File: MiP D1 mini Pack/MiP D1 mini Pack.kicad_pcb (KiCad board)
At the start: 2 copper layers, 41.4 x 63.8 mm, 15 parts, among them J1 MiP, J2 Debug, U1 WEMOS D1 mini, U2 74LVC1G125

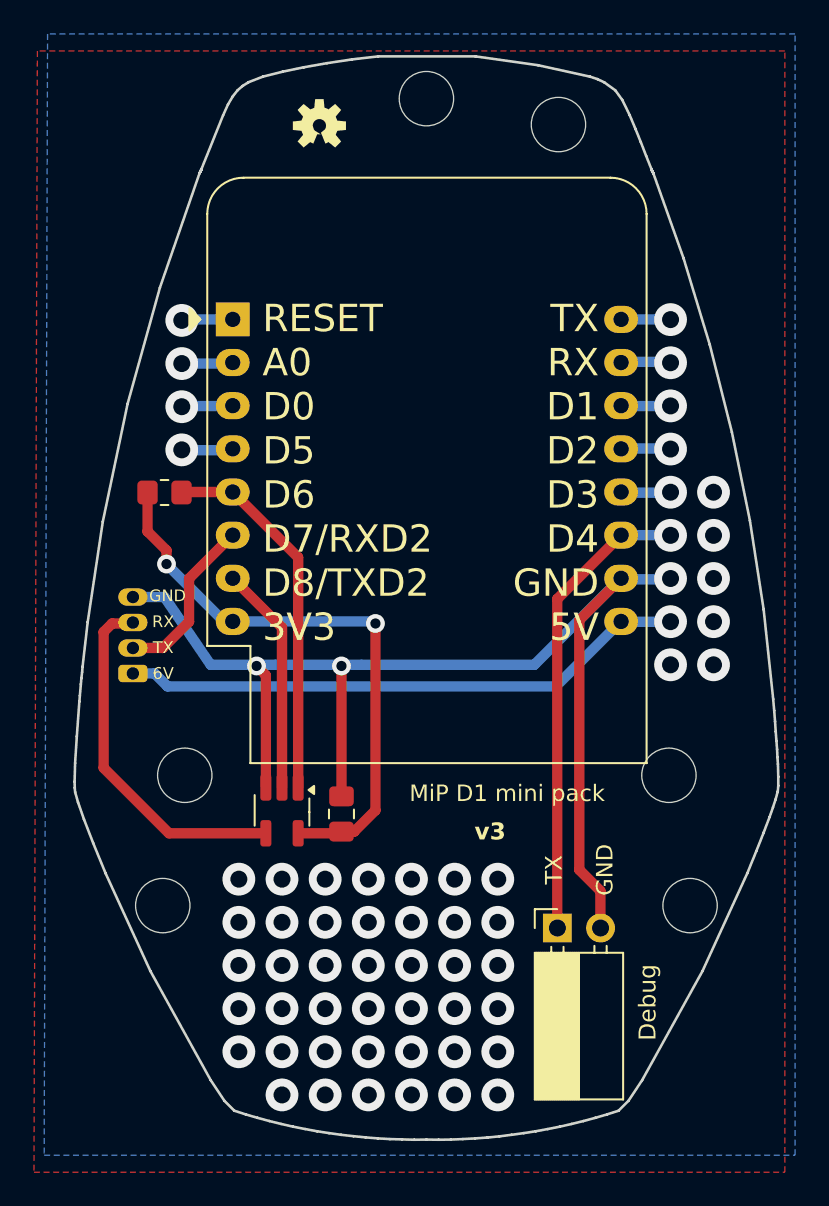
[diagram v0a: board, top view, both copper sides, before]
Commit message: Prototyping area
Figured out adding prototyping areas.
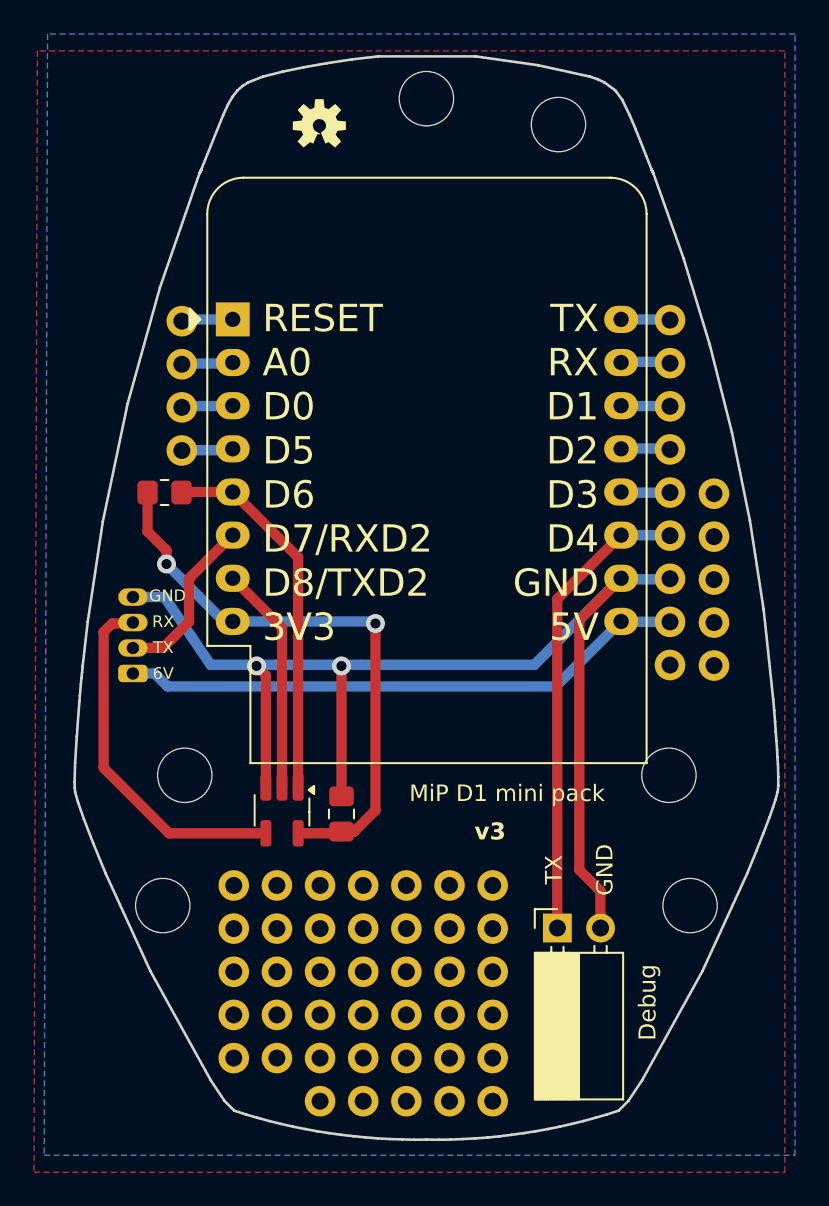
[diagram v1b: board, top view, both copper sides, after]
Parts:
- added REF**: Prototype pad, Tiogaplanet_Library:Prototype pad, F.Cu at (144.8, 124.5)
- added REF**: Prototype pad, Tiogaplanet_Library:Prototype pad, F.Cu at (139.7, 132.1)
- added REF**: Prototype pad, Tiogaplanet_Library:Prototype pad, F.Cu at (139.7, 129.5)
- added REF**: Prototype pad, Tiogaplanet_Library:Prototype pad, F.Cu at (134.1, 96.3)
- added REF**: Prototype pad, Tiogaplanet_Library:Prototype pad, F.Cu at (139.7, 121.9)
- added REF**: Prototype pad, Tiogaplanet_Library:Prototype pad, F.Cu at (144.8, 132.1)
- added REF**: Prototype pad, Tiogaplanet_Library:Prototype pad, F.Cu at (149.9, 121.9)
- added REF**: Prototype pad, Tiogaplanet_Library:Prototype pad, F.Cu at (149.9, 127.0)
- added REF**: Prototype pad, Tiogaplanet_Library:Prototype pad, F.Cu at (139.7, 124.5)
- added REF**: Prototype pad, Tiogaplanet_Library:Prototype pad, F.Cu at (152.4, 124.5)
- added REF**: Prototype pad, Tiogaplanet_Library:Prototype pad, F.Cu at (137.2, 124.5)
- added REF**: Prototype pad, Tiogaplanet_Library:Prototype pad, F.Cu at (162.8, 101.3)
- added REF**: Prototype pad, Tiogaplanet_Library:Prototype pad, F.Cu at (144.8, 121.9)
- added REF**: Prototype pad, Tiogaplanet_Library:Prototype pad, F.Cu at (165.4, 106.4)
- added REF**: Prototype pad, Tiogaplanet_Library:Prototype pad, F.Cu at (162.8, 108.9)
- added REF**: Prototype pad, Tiogaplanet_Library:Prototype pad, F.Cu at (152.4, 134.6)
- added REF**: Prototype pad, Tiogaplanet_Library:Prototype pad, F.Cu at (162.8, 88.6)
- added REF**: Prototype pad, Tiogaplanet_Library:Prototype pad, F.Cu at (144.8, 127.0)
- added REF**: Prototype pad, Tiogaplanet_Library:Prototype pad, F.Cu at (162.8, 91.2)
- added REF**: Prototype pad, Tiogaplanet_Library:Prototype pad, F.Cu at (152.4, 132.1)
- added REF**: Prototype pad, Tiogaplanet_Library:Prototype pad, F.Cu at (162.8, 93.7)
- added REF**: Prototype pad, Tiogaplanet_Library:Prototype pad, F.Cu at (149.9, 132.1)
- added REF**: Prototype pad, Tiogaplanet_Library:Prototype pad, F.Cu at (144.8, 129.5)
- added REF**: Prototype pad, Tiogaplanet_Library:Prototype pad, F.Cu at (142.2, 134.6)
- added REF**: Prototype pad, Tiogaplanet_Library:Prototype pad, F.Cu at (147.3, 124.5)
- added REF**: Prototype pad, Tiogaplanet_Library:Prototype pad, F.Cu at (147.3, 121.9)
- added REF**: Prototype pad, Tiogaplanet_Library:Prototype pad, F.Cu at (165.4, 109.0)
- added REF**: Prototype pad, Tiogaplanet_Library:Prototype pad, F.Cu at (162.8, 98.8)
- added REF**: Prototype pad, Tiogaplanet_Library:Prototype pad, F.Cu at (147.3, 129.5)
- added REF**: Prototype pad, Tiogaplanet_Library:Prototype pad, F.Cu at (134.1, 93.8)
- added REF**: Prototype pad, Tiogaplanet_Library:Prototype pad, F.Cu at (147.3, 132.1)
- added REF**: Prototype pad, Tiogaplanet_Library:Prototype pad, F.Cu at (162.8, 103.9)
- added REF**: Prototype pad, Tiogaplanet_Library:Prototype pad, F.Cu at (147.3, 127.0)
- added REF**: Prototype pad, Tiogaplanet_Library:Prototype pad, F.Cu at (137.2, 129.5)
- added REF**: Prototype pad, Tiogaplanet_Library:Prototype pad, F.Cu at (142.2, 121.9)
- added REF**: Prototype pad, Tiogaplanet_Library:Prototype pad, F.Cu at (139.7, 127.0)
- added REF**: Prototype pad, Tiogaplanet_Library:Prototype pad, F.Cu at (149.9, 124.5)
- added REF**: Prototype pad, Tiogaplanet_Library:Prototype pad, F.Cu at (149.9, 134.6)
- added REF**: Prototype pad, Tiogaplanet_Library:Prototype pad, F.Cu at (152.4, 121.9)
- added REF**: Prototype pad, Tiogaplanet_Library:Prototype pad, F.Cu at (137.2, 121.9)
- added REF**: Prototype pad, Tiogaplanet_Library:Prototype pad, F.Cu at (137.2, 132.1)
- added REF**: Prototype pad, Tiogaplanet_Library:Prototype pad, F.Cu at (147.3, 134.6)
- added REF**: Prototype pad, Tiogaplanet_Library:Prototype pad, F.Cu at (142.2, 129.5)
- added REF**: Prototype pad, Tiogaplanet_Library:Prototype pad, F.Cu at (152.4, 129.5)
- added REF**: Prototype pad, Tiogaplanet_Library:Prototype pad, F.Cu at (137.2, 127.0)
- added REF**: Prototype pad, Tiogaplanet_Library:Prototype pad, F.Cu at (165.4, 103.9)
- added REF**: Prototype pad, Tiogaplanet_Library:Prototype pad, F.Cu at (165.4, 101.4)
- added REF**: Prototype pad, Tiogaplanet_Library:Prototype pad, F.Cu at (142.2, 132.1)
- added REF**: Prototype pad, Tiogaplanet_Library:Prototype pad, F.Cu at (134.1, 91.2)
- added REF**: Prototype pad, Tiogaplanet_Library:Prototype pad, F.Cu at (149.9, 129.5)
- added REF**: Prototype pad, Tiogaplanet_Library:Prototype pad, F.Cu at (142.2, 127.0)
- added REF**: Prototype pad, Tiogaplanet_Library:Prototype pad, F.Cu at (142.2, 124.5)
- added REF**: Prototype pad, Tiogaplanet_Library:Prototype pad, F.Cu at (162.8, 106.4)
- added REF**: Prototype pad, Tiogaplanet_Library:Prototype pad, F.Cu at (134.1, 88.7)
- added REF**: Prototype pad, Tiogaplanet_Library:Prototype pad, F.Cu at (162.8, 96.3)
- added REF**: Prototype pad, Tiogaplanet_Library:Prototype pad, F.Cu at (144.8, 134.6)
- added REF**: Prototype pad, Tiogaplanet_Library:Prototype pad, F.Cu at (165.4, 98.9)
- added REF**: Prototype pad, Tiogaplanet_Library:Prototype pad, F.Cu at (152.4, 127.0)
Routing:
- net unconnected-(U1-~{RST}-Pad1): track 3.02 -> 2.94 mm, vias 1 -> 0
- net unconnected-(U1-TX-Pad16): vias 1 -> 0
- net unconnected-(U1-SDA/D2-Pad13): vias 1 -> 0
- net unconnected-(U1-SCL/D1-Pad14): vias 1 -> 0
- net unconnected-(U1-SCK/D5-Pad4): vias 1 -> 0
- net unconnected-(U1-RX-Pad15): vias 1 -> 0
- net unconnected-(U1-D3-Pad12): vias 1 -> 0
- net unconnected-(U1-D0-Pad3): vias 1 -> 0
- net unconnected-(U1-A0-Pad2): vias 1 -> 0
- net GND: vias 4 -> 2
- net /Debug: vias 1 -> 0
- net +6V: vias 2 -> 0
- net (no net): vias 45 -> 0
